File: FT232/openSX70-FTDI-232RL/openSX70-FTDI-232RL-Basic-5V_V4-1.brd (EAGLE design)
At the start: 25.4 x 17.3 mm, 19 parts, among them IC1 FT232RQ, J1 687106183722, U1 FT232RLSSOP

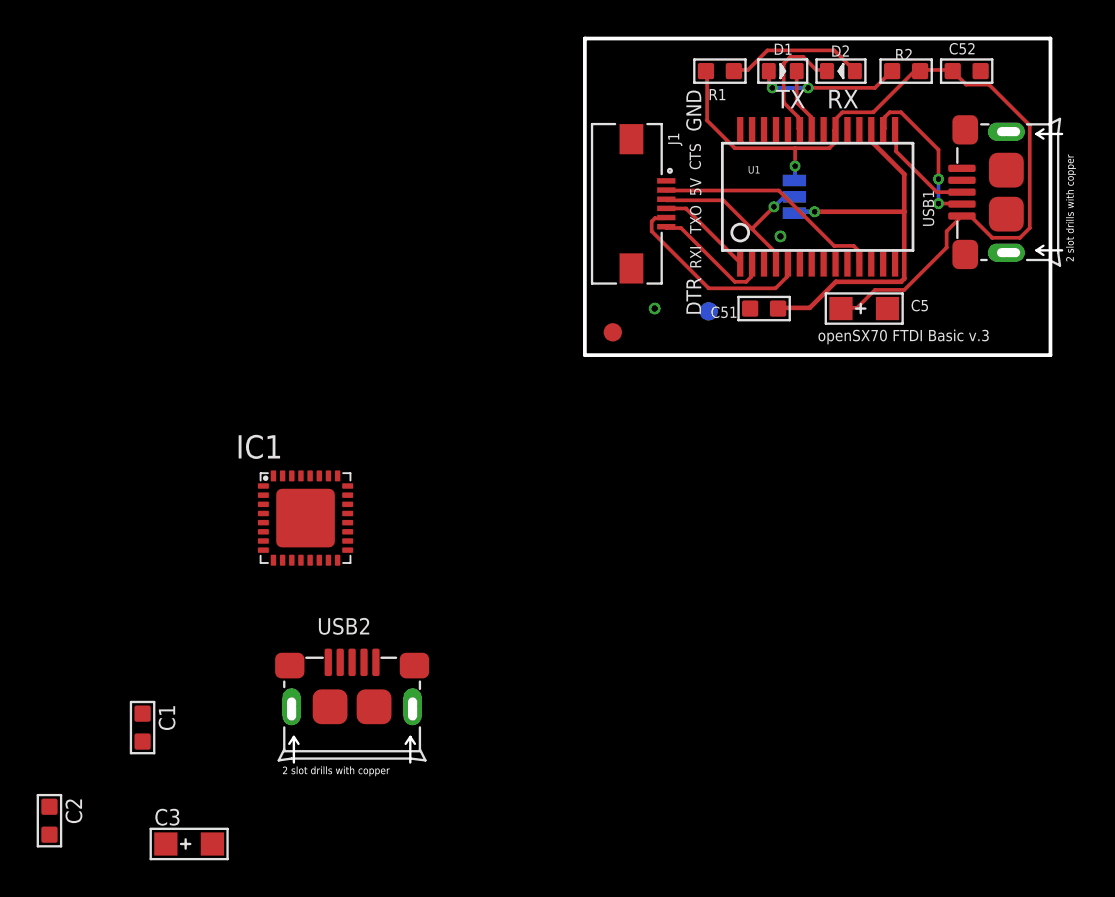
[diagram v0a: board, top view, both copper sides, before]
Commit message: New FTDI versions with FT232R L and Q
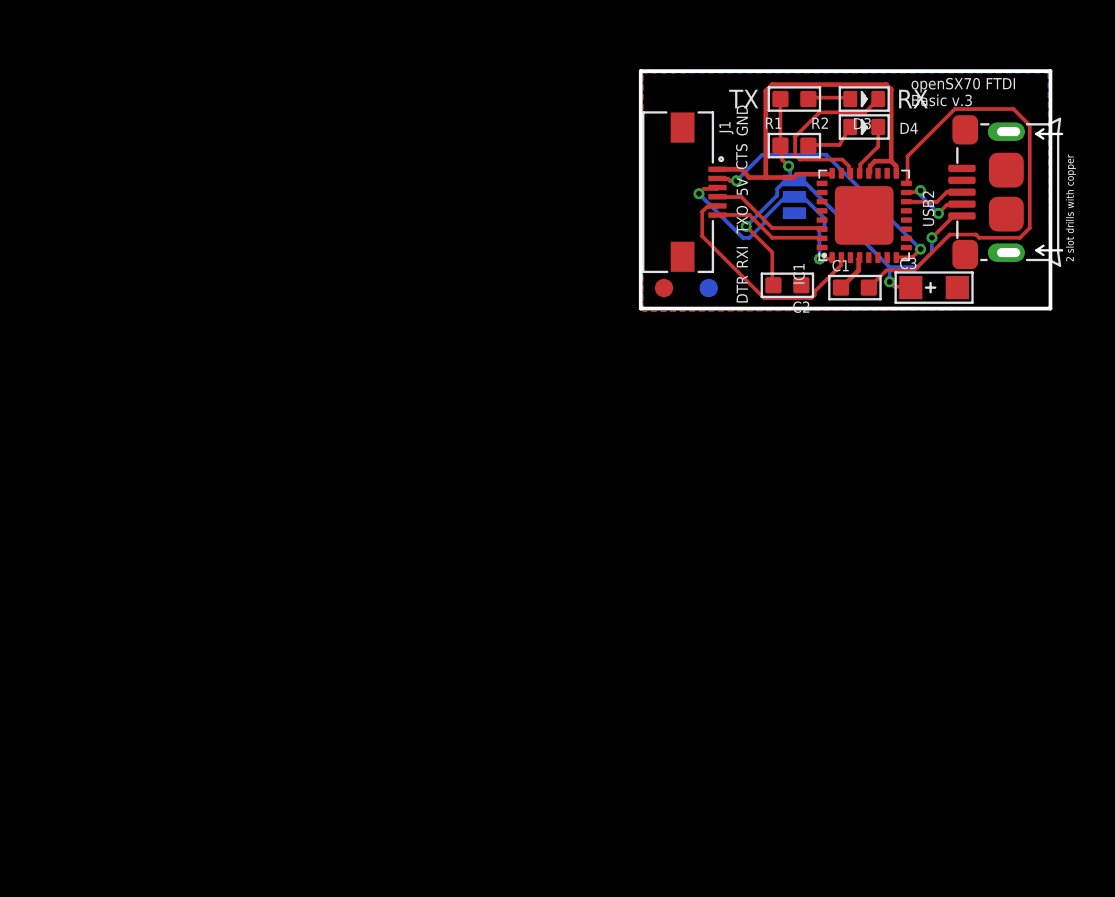
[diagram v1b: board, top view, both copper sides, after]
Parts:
- removed C5: 10uf, Seeed-Capacitor-2016:AVX-A
- removed C51, C52: 100nf, openSX70_PATHFINDER_V5.5-SEEED_20180522:C0603
- removed D1: GREEN-0603, Seeed-LED:LED-0603
- removed D2: YELLOW-0603, Seeed-LED-2016:LED-0603
- removed U1: FT232RLSSOP, SparkFun:SSOP28DB
- removed USB1: 10118193-0001LF, Seeed-Connector -2016:MICRO-USB5+6P-SMD-0.65-B
- added D3: YELLOW-0603, Seeed-LED-2016:LED-0603
- added D4: GREEN-0603, Seeed-LED:LED-0603
- moved C3 50.7 mm to (10.2, -5.21)
- moved C2 49.7 mm to (2.16, -5.08), turned to 270 degrees
- moved C1 45.7 mm to (5.84, -5.21), turned to 90 degrees
- moved USB2 41.7 mm to (11.4, 0.00), turned to 90 degrees
- moved IC1 34.7 mm to (6.35, -1.27), turned to 90 degrees
- moved R2 7.33 mm to (2.54, 2.54)
- moved R1 4.34 mm to (2.54, 5.08), turned to 90 degrees
- moved JP3 3.69 mm to (-4.57, -5.23)
- moved J1 2.87 mm to (-3.56, 0.00)
- moved JP5 1.27 mm to (-2.13, -5.23)
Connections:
- removed net N$1: D2.+, R1.1
- removed net N$2: D1.+, R2.1
- removed net N$3: U1.16, USB1.2
- removed net N$5: U1.7
- removed net RXLED: D1.-, U1.22
- removed net TXLED: D2.-, U1.23
- removed net USB_D+: U1.15, USB1.3
- new net N$10: D4.+, R2.2
- new net N$7: D3.-, IC1.22
- new net N$8: D4.-, IC1.21
- new net N$9: D3.+, R1.2
- net 3.3V: no longer C51.1, U1.17
- net 5V: now also R1.1, R2.1; no longer C5.+, C52.1, R1.2, R2.2, U1.20, USB1.1
- net CTS: no longer U1.11
- net DTR: no longer U1.2
- net GND: no longer C5.-, C51.2, C52.2, U1.18, U1.21, U1.25, U1.26, USB1.5, USB1.S1, USB1.S2, USB1.S3, USB1.S4, USB1.S5, USB1.S6
- net POWER: no longer U1.4
- net RXI: no longer U1.5
- net TXO: no longer U1.1
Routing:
- net GND: track 0.00 -> 26.8 mm, vias 2 -> 0
- net VCC: track 0.00 -> 25.5 mm
- net 3.3V: track 22.5 -> 0.00 mm, vias 1 -> 0
- net 5V: track 45.7 -> 27.4 mm, vias 1 -> 4
- net N$7: track 0.00 -> 10.0 mm
- net N$3: track 8.84 -> 0.00 mm, vias 2 -> 0
- net N$2: track 7.91 -> 0.00 mm, vias 2 -> 0
- net N$1: track 7.54 -> 0.00 mm
- net TXLED: track 6.82 -> 0.00 mm
- net USB_D+: track 5.73 -> 0.00 mm
- net N$4: track 0.00 -> 3.96 mm, vias 0 -> 2
- net RXLED: track 3.54 -> 0.00 mm
- net N$6: track 0.00 -> 3.25 mm
- net N$8: track 0.00 -> 2.94 mm
- net N$10: track 0.00 -> 2.85 mm
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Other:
- board size 25.4 x 17.3 mm -> 22.4 x 13 mm
